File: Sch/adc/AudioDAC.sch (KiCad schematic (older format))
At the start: 8 parts

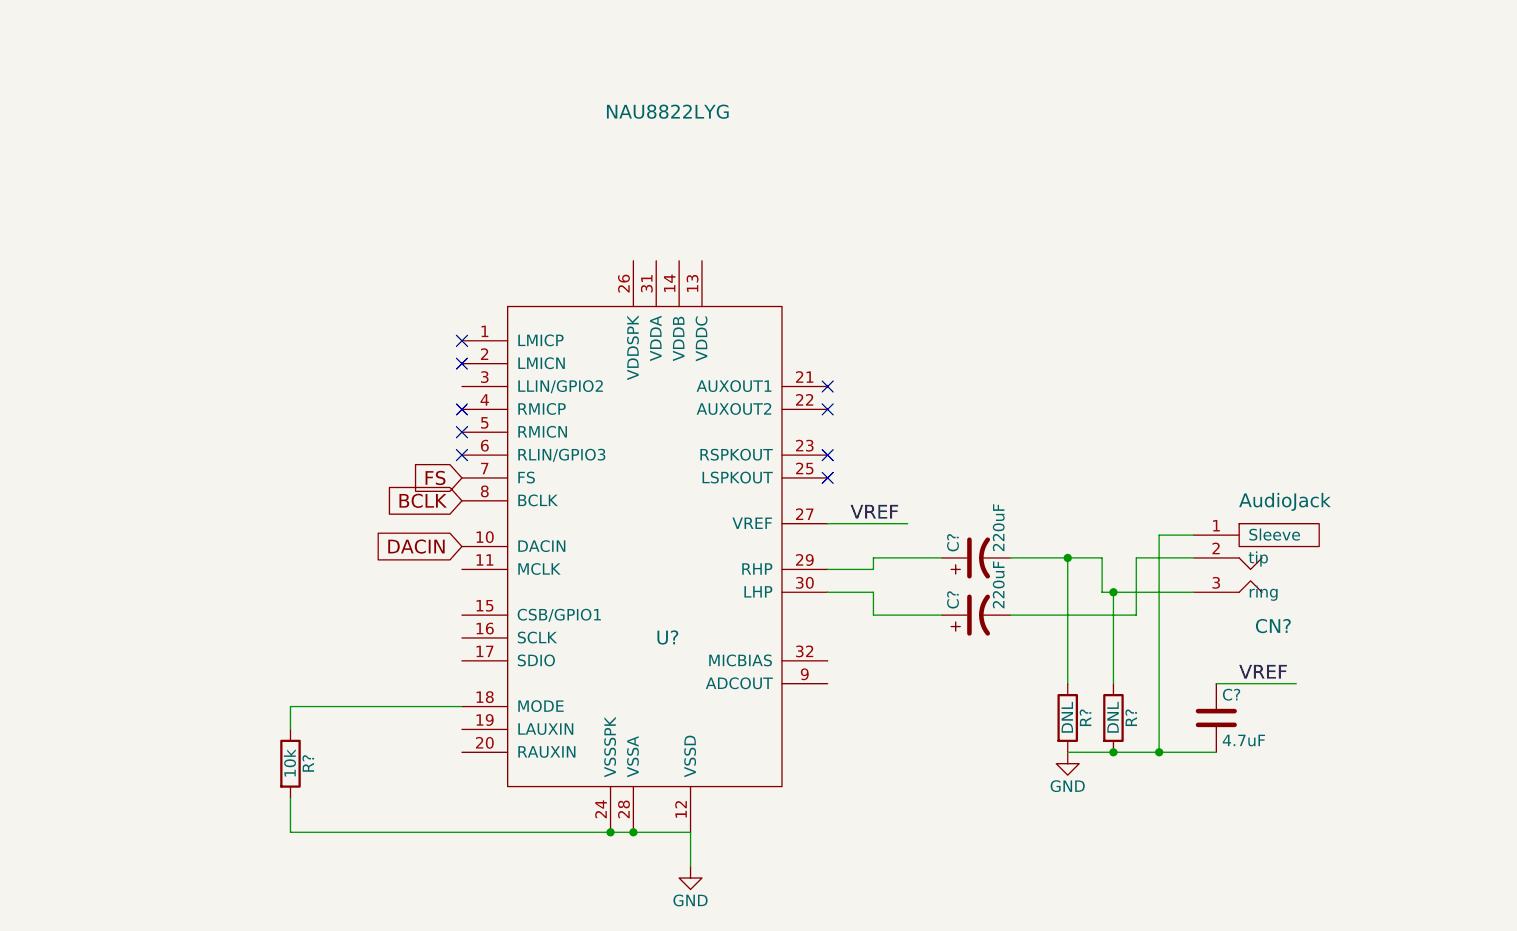
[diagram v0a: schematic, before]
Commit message: Audio DAC almost done. Is it OK to set VDDC=3.3V?
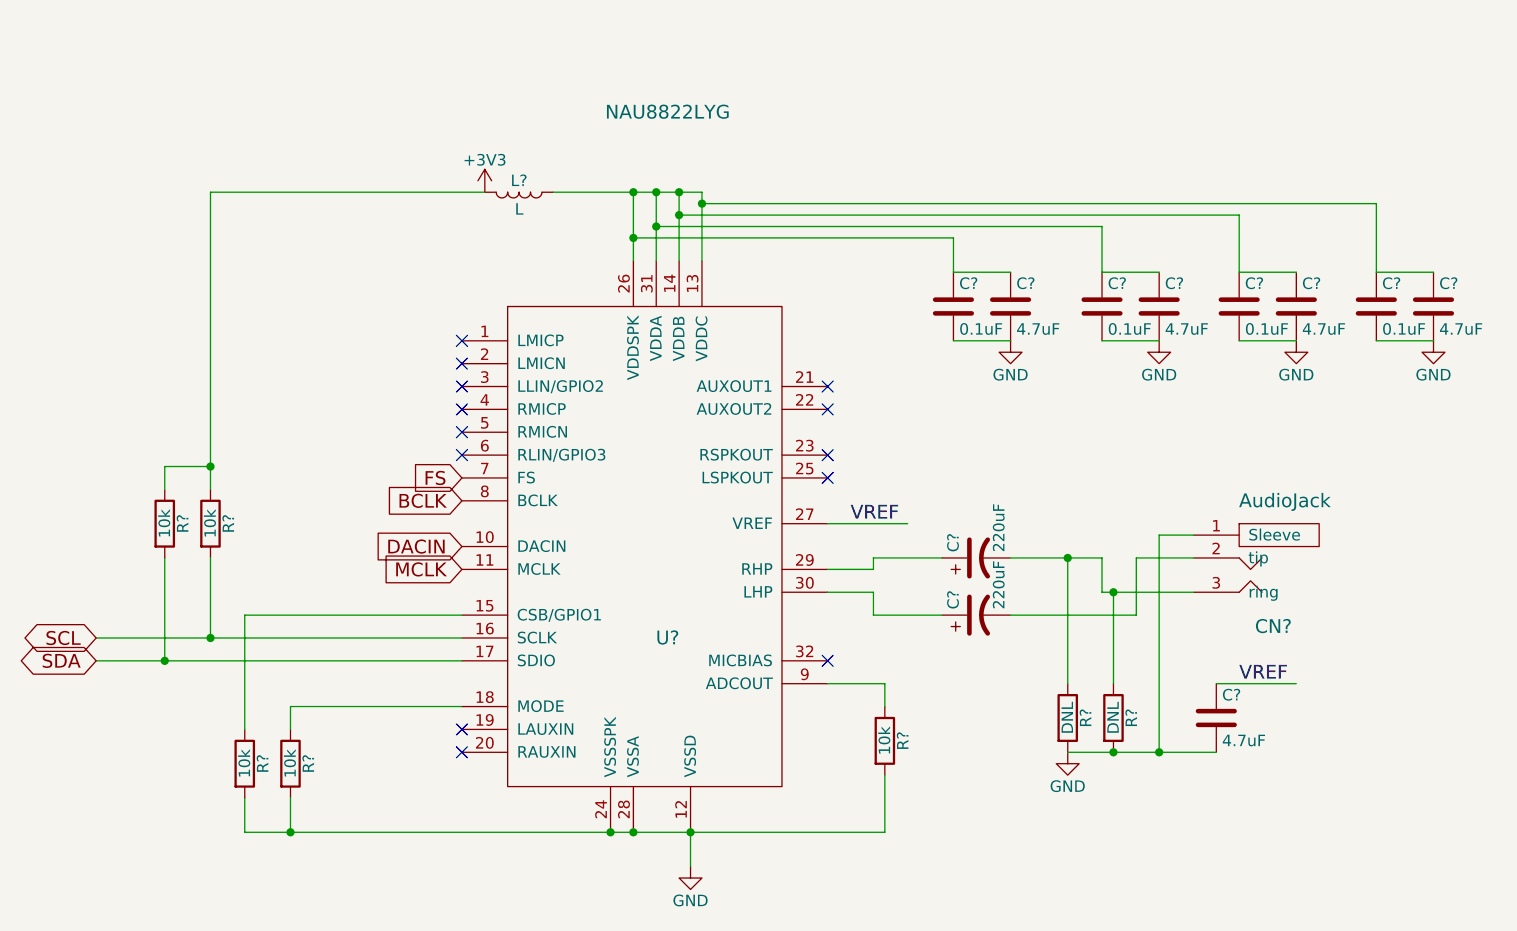
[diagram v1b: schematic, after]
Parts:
- added C? (x4): 4.7uF, symbol C
- added C? (x4): 0.1uF, symbol C
- added L?: L, symbol L
- added R? (x4): 10k, symbol R
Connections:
- net labels added: +3V3, MCLK, SCL, SDA
- wire segments 24 -> 59
- no-connect marks 9 -> 13

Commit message: Schematics done
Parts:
- added J7: JP2, symbol JP2
- gave numbers to parts that had none: 21
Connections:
- net labels added: VDD3
- wire segments 59 -> 62
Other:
- note added: "100mW"
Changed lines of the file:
@@
 $EndDescr
 $Comp
-L NAU8822LYG U?
+L NAU8822LYG U6
 U 1 1 58A94092
 P 5550 3250
-F 0 "U?" H 5550 2400 60  0000 C CNN
+F 0 "U6" H 5550 2400 60  0000 C CNN
 F 1 "NAU8822LYG" H 5550 4700 60  0000 C CNN
 F 2 "" H 5550 2400 60  0001 C CNN
@@
 $EndComp
 $Comp
-L AudioJack CN?
+L AudioJack CN3
 U 1 1 58A945B2
 P 8250 3750
-F 0 "CN?" H 8200 3450 60  0000 C CNN
+F 0 "CN3" H 8200 3450 60  0000 C CNN
 F 1 "AudioJack" H 8250 4000 60  0000 C CNN
 F 2 "" H 8200 3450 60  0001 C CNN
@@
 $EndComp
 $Comp
-L CP1 C?
+L CP1 C21
 U 1 1 58A94613
 P 6900 3750
-F 0 "C?" H 6925 3850 50  0000 L CNN
+F 0 "C21" H 6925 3850 50  0000 L CNN
 F 1 "220uF" H 6925 3650 50  0000 L CNN
 F 2 "" H 6900 3750 50  0000 C CNN
@@
 $EndComp
 $Comp
-L CP1 C?
+L CP1 C27
 U 1 1 58A94914
 P 6900 4000
-F 0 "C?" H 6925 4100 50  0000 L CNN
+F 0 "C27" H 6925 4100 50  0000 L CNN
 F 1 "220uF" H 6925 3900 50  0000 L CNN
 F 2 "" H 6900 4000 50  0000 C CNN
@@
 $EndComp
 $Comp
-L GND #PWR?
+L GND #PWR051
 U 1 1 58A94BF7
 P 7300 4600
-F 0 "#PWR?" H 7300 4350 50  0001 C CNN
+F 0 "#PWR051" H 7300 4350 50  0001 C CNN
 F 1 "GND" H 7300 4450 50  0000 C CNN
 F 2 "" H 7300 4600 50  0000 C CNN
@@
 $EndComp
 $Comp
-L R R?
+L R R29
 U 1 1 58A94C13
 P 7300 4450
-F 0 "R?" V 7380 4450 50  0000 C CNN
+F 0 "R29" V 7380 4450 50  0000 C CNN
 F 1 "DNL" V 7300 4450 50  0000 C CNN
 F 2 "" V 7230 4450 50  0000 C CNN
@@
 $EndComp
 $Comp
-L R R?
+L R R30
 U 1 1 58A94C87
 P 7500 4450
-F 0 "R?" V 7580 4450 50  0000 C CNN
+F 0 "R30" V 7580 4450 50  0000 C CNN
 F 1 "DNL" V 7500 4450 50  0000 C CNN
 F 2 "" V 7430 4450 50  0000 C CNN
@@
 VREF
 $Comp
-L C C?
+L C C43
 U 1 1 58A95D2B
 P 7950 4450
-F 0 "C?" H 7975 4550 50  0000 L CNN
+F 0 "C43" H 7975 4550 50  0000 L CNN
 F 1 "4.7uF" H 7975 4350 50  0000 L CNN
 F 2 "" H 7988 4300 50  0000 C CNN
@@
 $EndComp
 $Comp
-L GND #PWR?
+L GND #PWR052
 U 1 1 58A96033
 P 5650 5100
-F 0 "#PWR?" H 5650 4850 50  0001 C CNN
+F 0 "#PWR052" H 5650 4850 50  0001 C CNN
 F 1 "GND" H 5650 4950 50  0000 C CNN
 F 2 "" H 5650 5100 50  0000 C CNN
@@
 DACIN
 $Comp
-L R R?
+L R R27
 U 1 1 58A97C3B
 P 3900 4650
-F 0 "R?" V 3980 4650 50  0000 C CNN
+F 0 "R27" V 3980 4650 50  0000 C CNN
 F 1 "10k" V 3900 4650 50  0000 C CNN
 F 2 "" V 3830 4650 50  0000 C CNN
@@
 $EndComp
 $Comp
-L +3V3 #PWR?
+L +3V3 #PWR053
 U 1 1 58A98414
 P 4750 2150
-F 0 "#PWR?" H 4750 2000 50  0001 C CNN
+F 0 "#PWR053" H 4750 2000 50  0001 C CNN
 F 1 "+3V3" H 4750 2290 50  0000 C CNN
 F 2 "" H 4750 2150 50  0000 C CNN
@@
 $EndComp
 $Comp
-L L L?
+L L L8
 U 1 1 58A98450
 P 4900 2150
-F 0 "L?" V 4850 2150 50  0000 C CNN
+F 0 "L8" V 4850 2150 50  0000 C CNN
 F 1 "L" V 4975 2150 50  0000 C CNN
 F 2 "" H 4900 2150 50  0000 C CNN
@@
 MCLK
 $Comp
-L C C?
+L C C28
 U 1 1 58A98E1F
 P 7050 2650
-F 0 "C?" H 7075 2750 50  0000 L CNN
+F 0 "C28" H 7075 2750 50  0000 L CNN
 F 1 "4.7uF" H 7075 2550 50  0000 L CNN
 F 2 "" H 7088 2500 50  0000 C CNN
@@
 $EndComp
 $Comp
-L GND #PWR?
+L GND #PWR054
 U 1 1 58A98E4C
 P 7050 2800
-F 0 "#PWR?" H 7050 2550 50  0001 C CNN
+F 0 "#PWR054" H 7050 2550 50  0001 C CNN
 F 1 "GND" H 7050 2650 50  0000 C CNN
 F 2 "" H 7050 2800 50  0000 C CNN
@@
 $EndComp
 $Comp
-L C C?
+L C C3
 U 1 1 58A99163
 P 6800 2650
-F 0 "C?" H 6825 2750 50  0000 L CNN
+F 0 "C3" H 6825 2750 50  0000 L CNN
 F 1 "0.1uF" H 6825 2550 50  0000 L CNN
 F 2 "" H 6838 2500 50  0000 C CNN
@@
 $EndComp
 $Comp
-L C C?
+L C C42
 U 1 1 58A99752
 P 7700 2650
-F 0 "C?" H 7725 2750 50  0000 L CNN
+F 0 "C42" H 7725 2750 50  0000 L CNN
 F 1 "4.7uF" H 7725 2550 50  0000 L CNN
 F 2 "" H 7738 2500 50  0000 C CNN
@@
 $EndComp
 $Comp
-L GND #PWR?
+L GND #PWR055
 U 1 1 58A99758
 P 7700 2800
-F 0 "#PWR?" H 7700 2550 50  0001 C CNN
+F 0 "#PWR055" H 7700 2550 50  0001 C CNN
 F 1 "GND" H 7700 2650 50  0000 C CNN
 F 2 "" H 7700 2800 50  0000 C CNN
@@
 $EndComp
 $Comp
-L C C?
+L C C41
 U 1 1 58A9975E
 P 7450 2650
-F 0 "C?" H 7475 2750 50  0000 L CNN
+F 0 "C41" H 7475 2750 50  0000 L CNN
 F 1 "0.1uF" H 7475 2550 50  0000 L CNN
 F 2 "" H 7488 2500 50  0000 C CNN
@@
 $EndComp
 $Comp
-L C C?
+L C C45
 U 1 1 58A997A2
 P 8300 2650
-F 0 "C?" H 8325 2750 50  0000 L CNN
+F 0 "C45" H 8325 2750 50  0000 L CNN
 F 1 "4.7uF" H 8325 2550 50  0000 L CNN
 F 2 "" H 8338 2500 50  0000 C CNN
@@
 $EndComp
 $Comp
-L GND #PWR?
+L GND #PWR056
 U 1 1 58A997A8
 P 8300 2800
-F 0 "#PWR?" H 8300 2550 50  0001 C CNN
+F 0 "#PWR056" H 8300 2550 50  0001 C CNN
 F 1 "GND" H 8300 2650 50  0000 C CNN
 F 2 "" H 8300 2800 50  0000 C CNN
@@
 $EndComp
 $Comp
-L C C?
+L C C44
 U 1 1 58A997AE
 P 8050 2650
-F 0 "C?" H 8075 2750 50  0000 L CNN
+F 0 "C44" H 8075 2750 50  0000 L CNN
 F 1 "0.1uF" H 8075 2550 50  0000 L CNN
 F 2 "" H 8088 2500 50  0000 C CNN
@@
 $EndComp
 $Comp
-L C C?
+L C C47
 U 1 1 58A997FE
 P 8900 2650
-F 0 "C?" H 8925 2750 50  0000 L CNN
+F 0 "C47" H 8925 2750 50  0000 L CNN
 F 1 "4.7uF" H 8925 2550 50  0000 L CNN
 F 2 "" H 8938 2500 50  0000 C CNN
@@
 $EndComp
 $Comp
-L GND #PWR?
+L GND #PWR057
 U 1 1 58A99804
 P 8900 2800
-F 0 "#PWR?" H 8900 2550 50  0001 C CNN
+F 0 "#PWR057" H 8900 2550 50  0001 C CNN
 F 1 "GND" H 8900 2650 50  0000 C CNN
 F 2 "" H 8900 2800 50  0000 C CNN
@@
 $EndComp
 $Comp
-L C C?
+L C C46
 U 1 1 58A9980A
 P 8650 2650
-F 0 "C?" H 8675 2750 50  0000 L CNN
+F 0 "C46" H 8675 2750 50  0000 L CNN
 F 1 "0.1uF" H 8675 2550 50  0000 L CNN
 F 2 "" H 8688 2500 50  0000 C CNN
@@
 SDA
 $Comp
-L R R?
+L R R23
 U 1 1 58A9A860
 P 3700 4650
-F 0 "R?" V 3780 4650 50  0000 C CNN
+F 0 "R23" V 3780 4650 50  0000 C CNN
 F 1 "10k" V 3700 4650 50  0000 C CNN
 F 2 "" V 3630 4650 50  0000 C CNN
@@
 Connection ~ 5300 4950
 Wire Wire Line
-	5050 2150 5700 2150
+	5050 2150 6750 2150
 Wire Wire Line
 	5400 2150 5400 2450
@@
 Wire Wire Line
 	8650 2500 8900 2500
-Wire Wire Line
-	5700 2150 5700 2450
 Connection ~ 5600 2150
 Wire Wire Line
-	5700 2200 8650 2200
-Wire Wire Line
-	8650 2200 8650 2500
-Connection ~ 5700 2200
+	8650 1650 8650 2500
 Wire Wire Line
 	5600 2250 8050 2250
@@
 NoConn ~ 6250 4200
 $Comp
-L R R?
+L R R28
 U 1 1 58A9AF59
 P 6500 4550
-F 0 "R?" V 6580 4550 50  0000 C CNN
+F 0 "R28" V 6580 4550 50  0000 C CNN
 F 1 "10k" V 6500 4550 50  0000 C CNN
 F 2 "" V 6430 4550 50  0000 C CNN
@@
 	3050 4200 4650 4200
 $Comp
-L R R?
+L R R22
 U 1 1 58A9C32A
 P 3550 3600
-F 0 "R?" V 3630 3600 50  0000 C CNN
+F 0 "R22" V 3630 3600 50  0000 C CNN
 F 1 "10k" V 3550 3600 50  0000 C CNN
 F 2 "" V 3480 3600 50  0000 C CNN
@@
 $EndComp
 $Comp
-L R R?
+L R R21
 U 1 1 58A9C330
 P 3350 3600
-F 0 "R?" V 3430 3600 50  0000 C CNN
+F 0 "R21" V 3430 3600 50  0000 C CNN
 F 1 "10k" V 3350 3600 50  0000 C CNN
 F 2 "" V 3280 3600 50  0000 C CNN
@@
 	3350 3750 3350 4200
 Connection ~ 3350 4200
+Text GLabel 6750 1650 0    60   Input ~ 0
+VDD3
+$Comp
+L JP2 J7
+U 1 1 58A9B1E7
+P 7100 1650
+F 0 "J7" H 7100 1400 60  0000 C CNN
+F 1 "JP2" H 7100 1850 60  0000 C CNN
+F 2 "" H 7050 1750 60  0001 C CNN
+F 3 "" H 7050 1750 60  0001 C CNN
+	1    7100 1650
+	1    0    0    -1
+$EndComp
+Wire Wire Line
+	6750 2150 6750 1750
+Wire Wire Line
+	7450 1750 7450 1650
+Wire Wire Line
+	7450 1650 8650 1650
+Wire Wire Line
+	5700 2450 5700 2200
+Wire Wire Line
+	5700 2200 8650 2200
+Connection ~ 8650 2200
+Text Notes 4750 2600 0    60   ~ 0
+100mW
 $EndSCHEMATC

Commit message: Add netlist and BOM
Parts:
- C3: footprint (none) -> Capacitors_SMD:C_0402
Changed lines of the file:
@@
 F 0 "C21" H 6925 3850 50  0000 L CNN
 F 1 "220uF" H 6925 3650 50  0000 L CNN
-F 2 "" H 6900 3750 50  0000 C CNN
+F 2 "" H 6900 3750 50  0001 C CNN
 F 3 "" H 6900 3750 50  0000 C CNN
 	1    6900 3750
@@
 F 0 "C27" H 6925 4100 50  0000 L CNN
 F 1 "220uF" H 6925 3900 50  0000 L CNN
-F 2 "" H 6900 4000 50  0000 C CNN
+F 2 "" H 6900 4000 50  0001 C CNN
 F 3 "" H 6900 4000 50  0000 C CNN
 	1    6900 4000
@@
 F 0 "R29" V 7380 4450 50  0000 C CNN
 F 1 "DNL" V 7300 4450 50  0000 C CNN
-F 2 "" V 7230 4450 50  0000 C CNN
+F 2 "" V 7230 4450 50  0001 C CNN
 F 3 "" H 7300 4450 50  0000 C CNN
 	1    7300 4450
@@
 F 0 "R30" V 7580 4450 50  0000 C CNN
 F 1 "DNL" V 7500 4450 50  0000 C CNN
-F 2 "" V 7430 4450 50  0000 C CNN
+F 2 "" V 7430 4450 50  0001 C CNN
 F 3 "" H 7500 4450 50  0000 C CNN
 	1    7500 4450
@@
 F 0 "C43" H 7975 4550 50  0000 L CNN
 F 1 "4.7uF" H 7975 4350 50  0000 L CNN
-F 2 "" H 7988 4300 50  0000 C CNN
+F 2 "" H 7988 4300 50  0001 C CNN
 F 3 "" H 7950 4450 50  0000 C CNN
 	1    7950 4450
@@
 F 0 "R27" V 3980 4650 50  0000 C CNN
 F 1 "10k" V 3900 4650 50  0000 C CNN
-F 2 "" V 3830 4650 50  0000 C CNN
+F 2 "" V 3830 4650 50  0001 C CNN
 F 3 "" H 3900 4650 50  0000 C CNN
 	1    3900 4650
@@
 F 0 "L8" V 4850 2150 50  0000 C CNN
 F 1 "L" V 4975 2150 50  0000 C CNN
-F 2 "" H 4900 2150 50  0000 C CNN
+F 2 "" H 4900 2150 50  0001 C CNN
 F 3 "" H 4900 2150 50  0000 C CNN
 	1    4900 2150
@@
 F 0 "C28" H 7075 2750 50  0000 L CNN
 F 1 "4.7uF" H 7075 2550 50  0000 L CNN
-F 2 "" H 7088 2500 50  0000 C CNN
+F 2 "" H 7088 2500 50  0001 C CNN
 F 3 "" H 7050 2650 50  0000 C CNN
 	1    7050 2650
@@
 F 0 "C3" H 6825 2750 50  0000 L CNN
 F 1 "0.1uF" H 6825 2550 50  0000 L CNN
-F 2 "" H 6838 2500 50  0000 C CNN
+F 2 "Capacitors_SMD:C_0402" H 6838 2500 50  0001 C CNN
 F 3 "" H 6800 2650 50  0000 C CNN
 	1    6800 2650
@@
 F 0 "C42" H 7725 2750 50  0000 L CNN
 F 1 "4.7uF" H 7725 2550 50  0000 L CNN
-F 2 "" H 7738 2500 50  0000 C CNN
+F 2 "" H 7738 2500 50  0001 C CNN
 F 3 "" H 7700 2650 50  0000 C CNN
 	1    7700 2650
@@
 F 0 "C41" H 7475 2750 50  0000 L CNN
 F 1 "0.1uF" H 7475 2550 50  0000 L CNN
-F 2 "" H 7488 2500 50  0000 C CNN
+F 2 "" H 7488 2500 50  0001 C CNN
 F 3 "" H 7450 2650 50  0000 C CNN
 	1    7450 2650
@@
 F 0 "C45" H 8325 2750 50  0000 L CNN
 F 1 "4.7uF" H 8325 2550 50  0000 L CNN
-F 2 "" H 8338 2500 50  0000 C CNN
+F 2 "" H 8338 2500 50  0001 C CNN
 F 3 "" H 8300 2650 50  0000 C CNN
 	1    8300 2650
@@
 F 0 "C44" H 8075 2750 50  0000 L CNN
 F 1 "0.1uF" H 8075 2550 50  0000 L CNN
-F 2 "" H 8088 2500 50  0000 C CNN
+F 2 "" H 8088 2500 50  0001 C CNN
 F 3 "" H 8050 2650 50  0000 C CNN
 	1    8050 2650
@@
 F 0 "C47" H 8925 2750 50  0000 L CNN
 F 1 "4.7uF" H 8925 2550 50  0000 L CNN
-F 2 "" H 8938 2500 50  0000 C CNN
+F 2 "" H 8938 2500 50  0001 C CNN
 F 3 "" H 8900 2650 50  0000 C CNN
 	1    8900 2650
@@
 F 0 "C46" H 8675 2750 50  0000 L CNN
 F 1 "0.1uF" H 8675 2550 50  0000 L CNN
-F 2 "" H 8688 2500 50  0000 C CNN
+F 2 "" H 8688 2500 50  0001 C CNN
 F 3 "" H 8650 2650 50  0000 C CNN
 	1    8650 2650
@@
 F 0 "R23" V 3780 4650 50  0000 C CNN
 F 1 "10k" V 3700 4650 50  0000 C CNN
-F 2 "" V 3630 4650 50  0000 C CNN
+F 2 "" V 3630 4650 50  0001 C CNN
 F 3 "" H 3700 4650 50  0000 C CNN
 	1    3700 4650
@@
 F 0 "R28" V 6580 4550 50  0000 C CNN
 F 1 "10k" V 6500 4550 50  0000 C CNN
-F 2 "" V 6430 4550 50  0000 C CNN
+F 2 "" V 6430 4550 50  0001 C CNN
 F 3 "" H 6500 4550 50  0000 C CNN
 	1    6500 4550
@@
 F 0 "R22" V 3630 3600 50  0000 C CNN
 F 1 "10k" V 3550 3600 50  0000 C CNN
-F 2 "" V 3480 3600 50  0000 C CNN
+F 2 "" V 3480 3600 50  0001 C CNN
 F 3 "" H 3550 3600 50  0000 C CNN
 	1    3550 3600
@@
 F 0 "R21" V 3430 3600 50  0000 C CNN
 F 1 "10k" V 3350 3600 50  0000 C CNN
-F 2 "" V 3280 3600 50  0000 C CNN
+F 2 "" V 3280 3600 50  0001 C CNN
 F 3 "" H 3350 3600 50  0000 C CNN
 	1    3350 3600

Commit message: Adding parts
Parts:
- C21, C27: footprint (none) -> Capacitors_SMD:C_1206
- C28, C42, C43, C45, C47: footprint (none) -> Capacitors_SMD:C_0603
- C41, C44, C46: footprint (none) -> Capacitors_SMD:C_0402
- J7: footprint (none) -> Pin_Headers:Pin_Header_Straight_2x02_Pitch2.54mm
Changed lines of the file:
@@
 F 0 "C21" H 6925 3850 50  0000 L CNN
 F 1 "220uF" H 6925 3650 50  0000 L CNN
-F 2 "" H 6900 3750 50  0001 C CNN
+F 2 "Capacitors_SMD:C_1206" H 6900 3750 50  0001 C CNN
 F 3 "" H 6900 3750 50  0000 C CNN
 	1    6900 3750
@@
 F 0 "C27" H 6925 4100 50  0000 L CNN
 F 1 "220uF" H 6925 3900 50  0000 L CNN
-F 2 "" H 6900 4000 50  0001 C CNN
+F 2 "Capacitors_SMD:C_1206" H 6900 4000 50  0001 C CNN
 F 3 "" H 6900 4000 50  0000 C CNN
 	1    6900 4000
@@
 F 0 "C43" H 7975 4550 50  0000 L CNN
 F 1 "4.7uF" H 7975 4350 50  0000 L CNN
-F 2 "" H 7988 4300 50  0001 C CNN
+F 2 "Capacitors_SMD:C_0603" H 7988 4300 50  0001 C CNN
 F 3 "" H 7950 4450 50  0000 C CNN
 	1    7950 4450
@@
 F 0 "C28" H 7075 2750 50  0000 L CNN
 F 1 "4.7uF" H 7075 2550 50  0000 L CNN
-F 2 "" H 7088 2500 50  0001 C CNN
+F 2 "Capacitors_SMD:C_0603" H 7088 2500 50  0001 C CNN
 F 3 "" H 7050 2650 50  0000 C CNN
 	1    7050 2650
@@
 F 0 "C42" H 7725 2750 50  0000 L CNN
 F 1 "4.7uF" H 7725 2550 50  0000 L CNN
-F 2 "" H 7738 2500 50  0001 C CNN
+F 2 "Capacitors_SMD:C_0603" H 7738 2500 50  0001 C CNN
 F 3 "" H 7700 2650 50  0000 C CNN
 	1    7700 2650
@@
 F 0 "C41" H 7475 2750 50  0000 L CNN
 F 1 "0.1uF" H 7475 2550 50  0000 L CNN
-F 2 "" H 7488 2500 50  0001 C CNN
+F 2 "Capacitors_SMD:C_0402" H 7488 2500 50  0001 C CNN
 F 3 "" H 7450 2650 50  0000 C CNN
 	1    7450 2650
@@
 F 0 "C45" H 8325 2750 50  0000 L CNN
 F 1 "4.7uF" H 8325 2550 50  0000 L CNN
-F 2 "" H 8338 2500 50  0001 C CNN
+F 2 "Capacitors_SMD:C_0603" H 8338 2500 50  0001 C CNN
 F 3 "" H 8300 2650 50  0000 C CNN
 	1    8300 2650
@@
 F 0 "C44" H 8075 2750 50  0000 L CNN
 F 1 "0.1uF" H 8075 2550 50  0000 L CNN
-F 2 "" H 8088 2500 50  0001 C CNN
+F 2 "Capacitors_SMD:C_0402" H 8088 2500 50  0001 C CNN
 F 3 "" H 8050 2650 50  0000 C CNN
 	1    8050 2650
@@
 F 0 "C47" H 8925 2750 50  0000 L CNN
 F 1 "4.7uF" H 8925 2550 50  0000 L CNN
-F 2 "" H 8938 2500 50  0001 C CNN
+F 2 "Capacitors_SMD:C_0603" H 8938 2500 50  0001 C CNN
 F 3 "" H 8900 2650 50  0000 C CNN
 	1    8900 2650
@@
 F 0 "C46" H 8675 2750 50  0000 L CNN
 F 1 "0.1uF" H 8675 2550 50  0000 L CNN
-F 2 "" H 8688 2500 50  0001 C CNN
+F 2 "Capacitors_SMD:C_0402" H 8688 2500 50  0001 C CNN
 F 3 "" H 8650 2650 50  0000 C CNN
 	1    8650 2650
@@
 F 0 "J7" H 7100 1400 60  0000 C CNN
 F 1 "JP2" H 7100 1850 60  0000 C CNN
-F 2 "" H 7050 1750 60  0001 C CNN
+F 2 "Pin_Headers:Pin_Header_Straight_2x02_Pitch2.54mm" H 7050 1750 60  0001 C CNN
 F 3 "" H 7050 1750 60  0001 C CNN
 	1    7100 1650

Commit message: Add parts
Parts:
- R21, R22, R23, R27, R28, R29, R30: footprint (none) -> Resistors_SMD:R_0603
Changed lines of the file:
@@
 F 0 "R29" V 7380 4450 50  0000 C CNN
 F 1 "DNL" V 7300 4450 50  0000 C CNN
-F 2 "" V 7230 4450 50  0001 C CNN
+F 2 "Resistors_SMD:R_0603" V 7230 4450 50  0001 C CNN
 F 3 "" H 7300 4450 50  0000 C CNN
 	1    7300 4450
@@
 F 0 "R30" V 7580 4450 50  0000 C CNN
 F 1 "DNL" V 7500 4450 50  0000 C CNN
-F 2 "" V 7430 4450 50  0001 C CNN
+F 2 "Resistors_SMD:R_0603" V 7430 4450 50  0001 C CNN
 F 3 "" H 7500 4450 50  0000 C CNN
 	1    7500 4450
@@
 F 0 "R27" V 3980 4650 50  0000 C CNN
 F 1 "10k" V 3900 4650 50  0000 C CNN
-F 2 "" V 3830 4650 50  0001 C CNN
+F 2 "Resistors_SMD:R_0603" V 3830 4650 50  0001 C CNN
 F 3 "" H 3900 4650 50  0000 C CNN
 	1    3900 4650
@@
 F 0 "R23" V 3780 4650 50  0000 C CNN
 F 1 "10k" V 3700 4650 50  0000 C CNN
-F 2 "" V 3630 4650 50  0001 C CNN
+F 2 "Resistors_SMD:R_0603" V 3630 4650 50  0001 C CNN
 F 3 "" H 3700 4650 50  0000 C CNN
 	1    3700 4650
@@
 F 0 "R28" V 6580 4550 50  0000 C CNN
 F 1 "10k" V 6500 4550 50  0000 C CNN
-F 2 "" V 6430 4550 50  0001 C CNN
+F 2 "Resistors_SMD:R_0603" V 6430 4550 50  0001 C CNN
 F 3 "" H 6500 4550 50  0000 C CNN
 	1    6500 4550
@@
 F 0 "R22" V 3630 3600 50  0000 C CNN
 F 1 "10k" V 3550 3600 50  0000 C CNN
-F 2 "" V 3480 3600 50  0001 C CNN
+F 2 "Resistors_SMD:R_0603" V 3480 3600 50  0001 C CNN
 F 3 "" H 3550 3600 50  0000 C CNN
 	1    3550 3600
@@
 F 0 "R21" V 3430 3600 50  0000 C CNN
 F 1 "10k" V 3350 3600 50  0000 C CNN
-F 2 "" V 3280 3600 50  0001 C CNN
+F 2 "Resistors_SMD:R_0603" V 3280 3600 50  0001 C CNN
 F 3 "" H 3350 3600 50  0000 C CNN
 	1    3350 3600
